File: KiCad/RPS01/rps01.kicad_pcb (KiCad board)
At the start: 2 copper layers, 150 x 80 mm, 43 parts, among them J1 Battery1, J2 Battery2, J3 ESC Output, J4 Conn_01x02_Socket, Q1 NMOS, Q2 NMOS, Q3 NMOS, Q4 NMOS, U1 LTC3780EG-TRPBF, U2 LTC4416EMS-1-TRPBF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

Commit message: cleanup
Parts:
- J1: value Battery1 -> XT90 BAT1
- J2: value Battery2 -> XT90 BAT2
- J3: value ESC Output -> XT90 ESC Output
- J4: value Conn_01x02_Socket -> XT30 Horizontal
- moved J3 25.2 mm to (22.9, 52.2), turned to -90 degrees
- moved U2 0.40 mm to (35.8, 56.6)
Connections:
- Cin(b)1 pad 1: /19V Boost/Vin -> /Load Sharing/VS
- Cin(c)1 pad 1: /19V Boost/Vin -> /Load Sharing/VS
- Q1 pad 1: /19V Boost/Vin -> /Load Sharing/VS
- Rin(Run)1 pad 1: /19V Boost/Vin -> /Load Sharing/VS
- U1 pad 21: /19V Boost/Vin -> /Load Sharing/VS
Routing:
- net /Load Sharing/G2: track 31.0 -> 0.00 mm, vias 2 -> 0
- net /Load Sharing/V1: track 24.7 -> 0.00 mm, vias 10 -> 0
- net /Load Sharing/G1: track 22.0 -> 0.00 mm, vias 2 -> 0
- net /Load Sharing/V2: track 22.0 -> 0.00 mm, vias 11 -> 0
- net GND: track 22.0 -> 0.00 mm, vias 1 -> 0
- net /Load Sharing/VS: track 14.8 -> 0.00 mm, vias 1 -> 0
- removed copper zone on B.Cu, net /Load Sharing/V1
- removed copper zone on F.Cu, net /Load Sharing/V1
- removed copper zone on B.Cu, net /Load Sharing/V2
- removed copper zone on F.Cu, net /Load Sharing/V2
- removed copper zone on B.Cu, net /Load Sharing/VS
- removed copper zone on F.Cu, net /Load Sharing/VS
- removed copper zone on B.Cu, net GND
- removed copper zone on F.Cu, net GND

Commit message: Updates
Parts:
- removed the REF** at (14.0, 13.5)
- added REF**: V0_PC100_Power_Board, Mechatronics Template:V0_PC100_Power_Board, F.Cu at (30.5, 28.1)
- moved J1 26.4 mm to (41.7, 47.0)
- moved J3 26.4 mm to (41.8, 70.7)
- moved U2 26.4 mm to (54.7, 75.1)
- moved U6 26.4 mm to (54.7, 62.5)
- moved J2 26.4 mm to (41.7, 106.5)
- moved U3 26.4 mm to (54.7, 51.5)
- moved U4 26.4 mm to (54.7, 89.6)
- moved U5 26.4 mm to (54.7, 102.5)
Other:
- board size 150 x 80 mm -> 150 x 100 mm

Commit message: update
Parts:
- removed REF**: V0_PC100_Power_Board, Mechatronics Template:V0_PC100_Power_Board
- added C1: 0.1mu, Capacitor_SMD:C_1206_3216Metric, F.Cu at (63.6, -41.4)
- added C2: 0.1mu, Capacitor_SMD:C_1206_3216Metric, F.Cu at (63.6, -38.1)
- added R1: 4.7k, Resistor_SMD:R_1206_3216Metric, F.Cu at (58.0, -46.2)
- added R2: 10k, Resistor_SMD:R_1206_3216Metric, F.Cu at (58.0, -42.9)
- added R3: 1k, Resistor_SMD:R_1206_3216Metric, F.Cu at (58.0, -39.6)
- added RL1: 72.3k, Resistor_SMD:R_1210_3225Metric, F.Cu at (63.6, -34.3)
- added Rs2: 0.5m, Resistor_SMD:R_1206_3216Metric, F.Cu at (58.0, -36.4)
- added U7: INA139NA/250, INA139:PW8, F.Cu at (58.5, -51.0)
- J3: footprint Mechatronic Footprints:AMASS_XT90-F_1x02_P11.00mm_Vertical -> AMASS XT90 Vertical:AMASS_XT90-M_1x02_P11.00mm_Vertical
- J4: value XT30 Horizontal -> XT30PW Horizontal; footprint Connector_AMASS:AMASS_XT60-F_1x02_P7.20mm_Vertical -> AMASS XT60-XT30:AMASS_XT30PW-F_1x02_P2.50mm_Horizontal
- U1: footprint Mechatronic Footprints:SSOP-24_G_LIT -> LTC3780:SSOP-24_G_LIT
- U2: footprint Mechatronic Footprints:MSOP-10_MS_LIT -> LTC4416:MSOP-10_MS_LIT
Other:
- board outline removed

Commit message: Updates
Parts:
- added J5: XT60 Vertical 12V, AMASS XT60-XT30:AMASS_XT60-M_1x02_P7.20mm_Vertical, F.Cu at (152.8, 64.3)
- added J6: XT60 Vertical 5V, AMASS XT60-XT30:AMASS_XT60-M_1x02_P7.20mm_Vertical, F.Cu at (152.8, 74.5)
- added J7: XT60 Vertical BATOUT, AMASS XT60-XT30:AMASS_XT60-M_1x02_P7.20mm_Vertical, F.Cu at (152.8, 84.8)
- added REF**: V0_PC100_Power_Board, Mechatronics Template:V0_PC100_Power_Board, F.Cu at (30.5, 28.7)
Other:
- board outline added: 150 x 100 mm

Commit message: .zip??
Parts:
- removed J5: XT60 Vertical 12V, AMASS XT60-XT30:AMASS_XT60-M_1x02_P7.20mm_Vertical
- removed J7: XT60 Vertical BATOUT, AMASS XT60-XT30:AMASS_XT60-M_1x02_P7.20mm_Vertical
- removed REF**: V0_PC100_Power_Board, Mechatronics Template:V0_PC100_Power_Board
- added D3: LED, LED_THT:LED_D5.0mm, F.Cu at (347.1, 60.8)
- added R6: 10K, Resistor_THT:R_Axial_DIN0204_L3.6mm_D1.6mm_P1.90mm_Vertical, F.Cu at (347.4, 47.0)
- added R7: 1k, Resistor_THT:R_Axial_DIN0204_L3.6mm_D1.6mm_P1.90mm_Vertical, F.Cu at (347.4, 50.1)
- added SW1: SW_Push_Open, Button_Switch_THT:SW_PUSH_6mm, F.Cu at (336.1, 59.1)
- added U8: ATmega328PB-A, Package_QFP:TQFP-32_7x7mm_P0.8mm, F.Cu at (339.9, 51.2)
- J4: footprint AMASS XT60-XT30:AMASS_XT30PW-F_1x02_P2.50mm_Horizontal -> Connector_AMASS:AMASS_XT60-F_1x02_P7.20mm_Vertical
- J6: value XT60 Vertical 5V -> 6pin; footprint AMASS XT60-XT30:AMASS_XT60-M_1x02_P7.20mm_Vertical -> Connector_PinHeader_2.54mm:PinHeader_2x03_P2.54mm_Vertical
- moved J6 191.9 mm to (344.7, 74.7)
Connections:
- J6 pad 1: unconnected-(J6-Pin_1-Pad1) -> GND
- J6 pad 2: unconnected-(J6-Pin_2-Pad2) -> Net-(J6-Pin_2)
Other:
- board outline removed

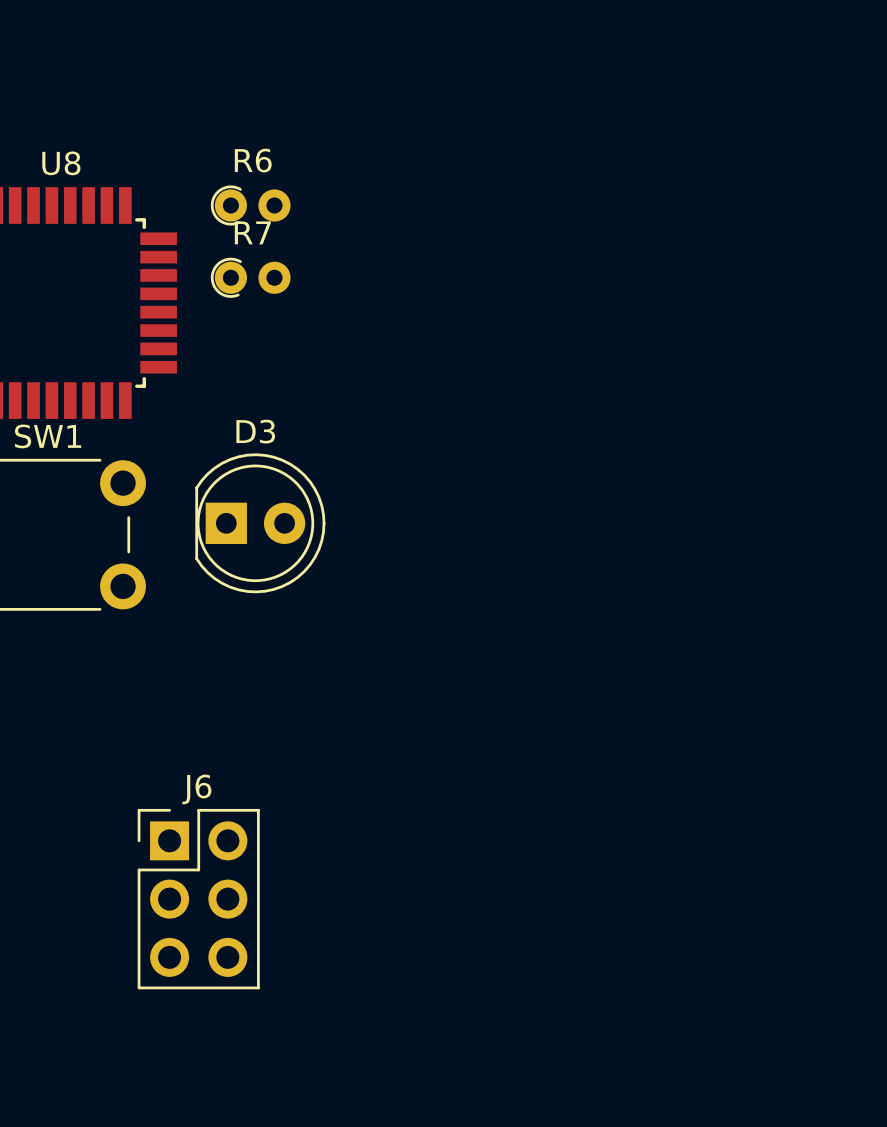
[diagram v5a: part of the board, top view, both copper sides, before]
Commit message: Add MCU to the root Kicad
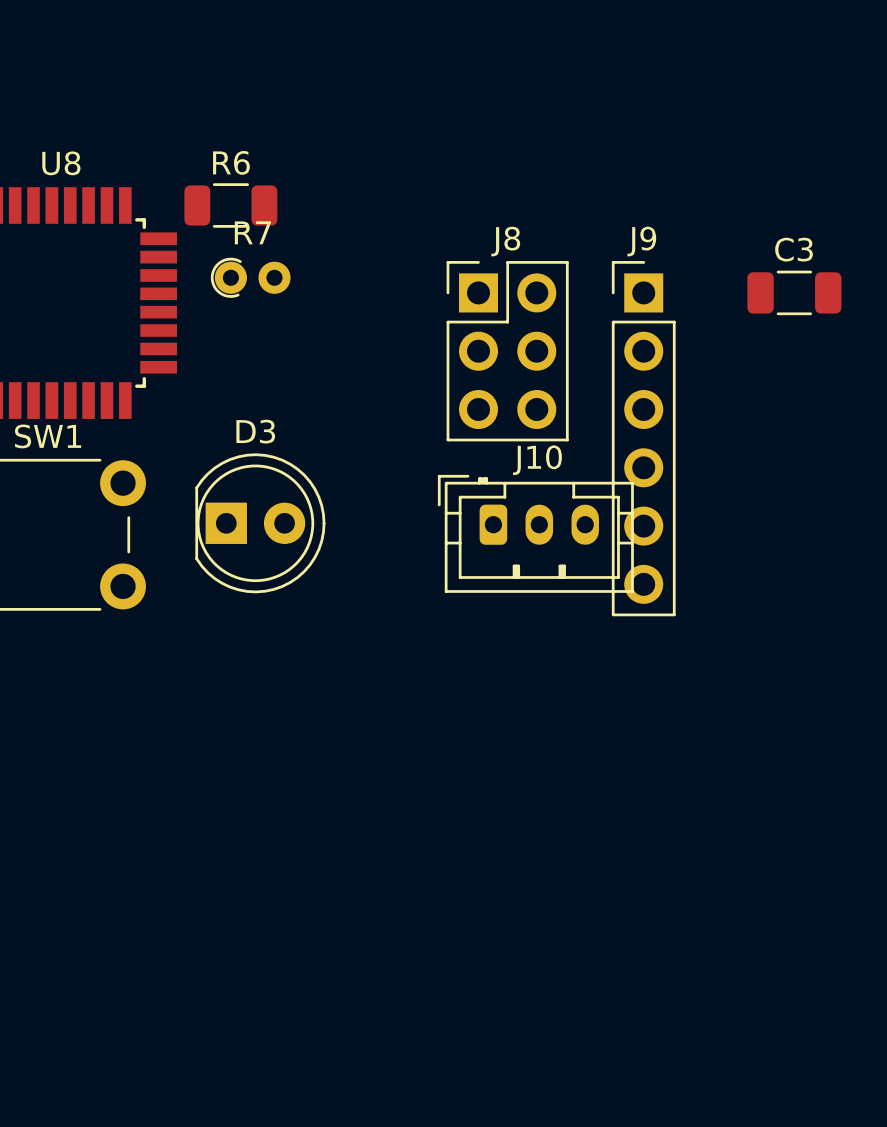
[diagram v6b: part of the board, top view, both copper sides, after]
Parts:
- removed J6: 6pin, Connector_PinHeader_2.54mm:PinHeader_2x03_P2.54mm_Vertical
- added C3: 100nF, Capacitor_SMD:C_1206_3216Metric, F.Cu at (371.9, 50.8)
- added J10: MCU_I2C_JSTGH3, Connector_JST:JST_PH_B3B-PH-K_1x03_P2.00mm_Vertical, F.Cu at (358.8, 60.9)
- added J8: MCU_ICSP_header, Connector_PinHeader_2.54mm:PinHeader_2x03_P2.54mm_Vertical, F.Cu at (358.1, 50.8)
- added J9: MCU_prog_header, Connector_PinHeader_2.54mm:PinHeader_1x06_P2.54mm_Vertical, F.Cu at (365.3, 50.8)
- D3: value LED -> MCU_LED
- R6: footprint Resistor_THT:R_Axial_DIN0204_L3.6mm_D1.6mm_P1.90mm_Vertical -> Resistor_SMD:R_1206_3216Metric
- SW1: value SW_Push_Open -> MCU_Button
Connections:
- net Net-(J6-Pin_2) renamed /Microcontroller/RESET
- U8 pad 15: MOSI -> /Microcontroller/MOSI
- U8 pad 16: MISO -> /Microcontroller/MISO
- U8 pad 17: SCK -> /Microcontroller/SCK
- U8 pad 30: unconnected-(U8-PD0-Pad30) -> /Microcontroller/RX
- U8 pad 31: unconnected-(U8-PD1-Pad31) -> /Microcontroller/TX
